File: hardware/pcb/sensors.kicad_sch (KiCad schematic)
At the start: 32 parts, among them J4 4-20mA_1, J5 4-20mA_2, J6 DS18B20, J7 Spare, Q2 BSS123, U9 ADS1115

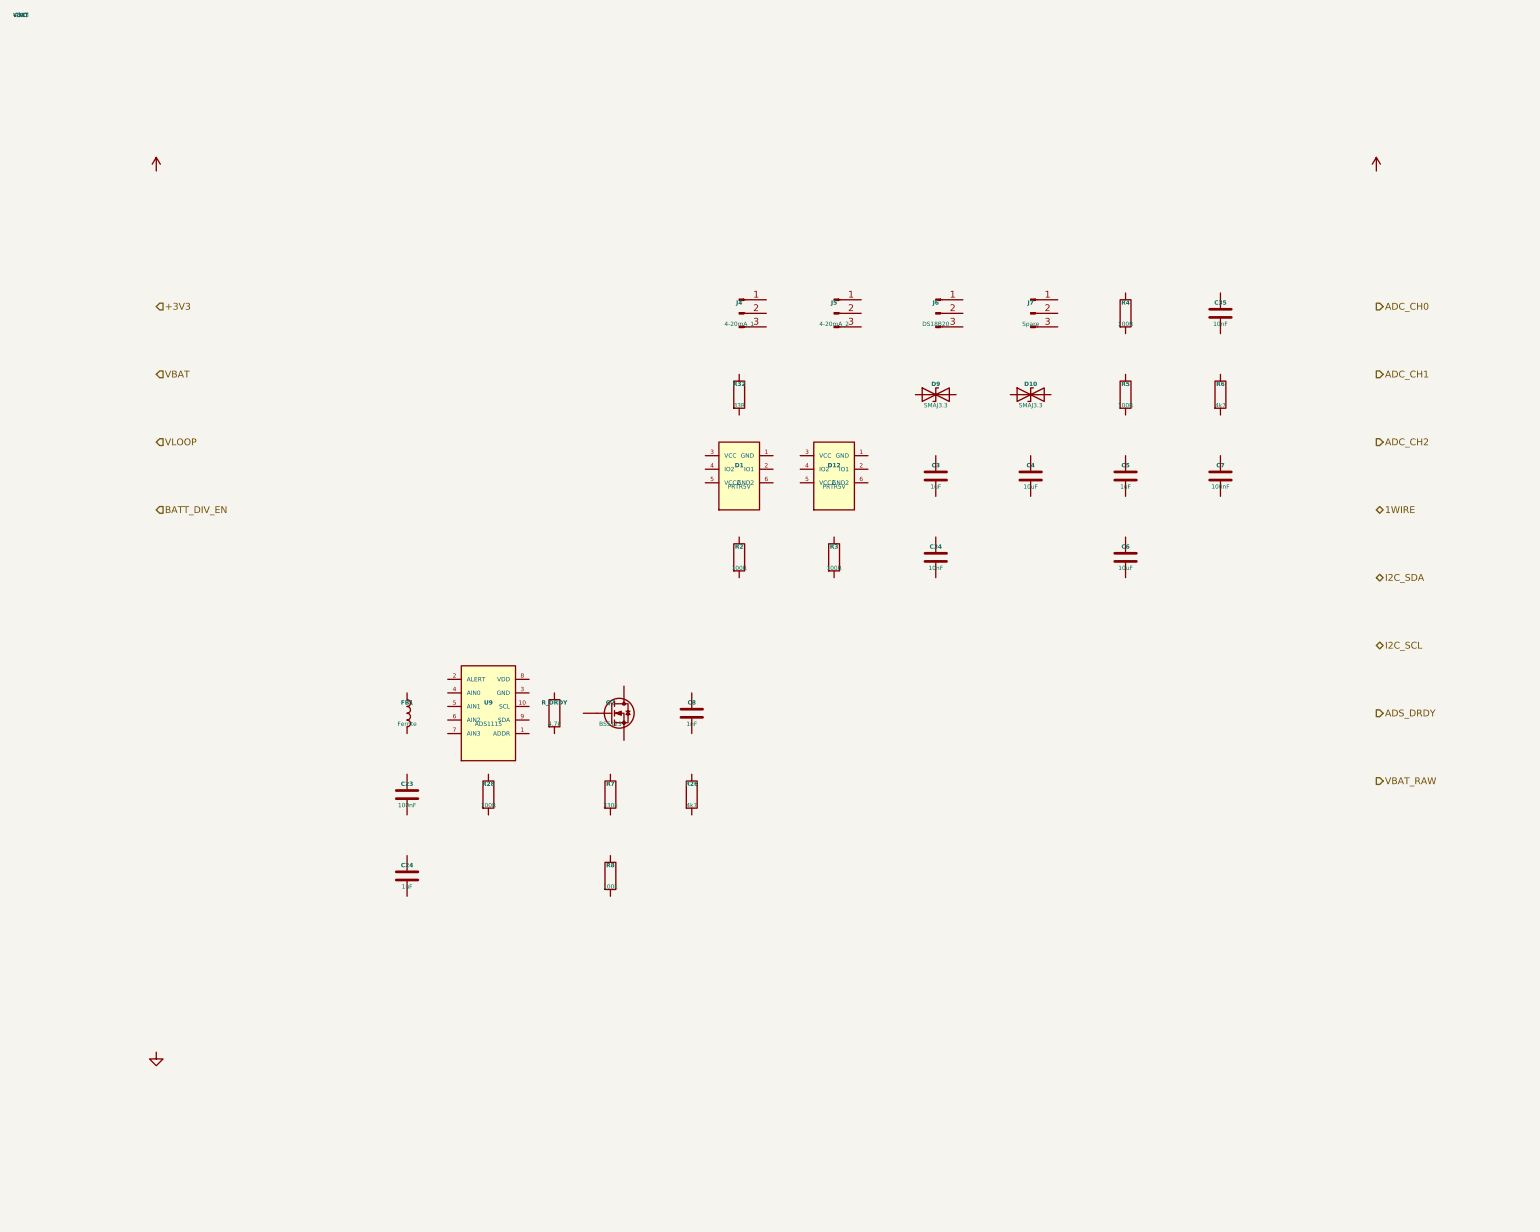
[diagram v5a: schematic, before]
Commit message: hw(pcb): wiring pass — schematic fully wired, netlist machine-verified (0 mismatches)
All four sheets wired with stub+label connectivity (434 wires, 21
explicit no-connects, PWR_FLAGs on undriven rails): power rails on
global labels, cross-sheet signals on hierarchical labels + rebuilt
top-sheet pins (24 hierarchical nets; vestigial ADC_CH* pins deleted,
GPIO14_LED corrected to the mcu-local net it really is), sheet-local
nets on local labels.

Verification (kicad-cli for the KiCad-10 format is not installable
here): hardware/pcb/kicad_wire_script.py generates the connectivity
from an embedded intent table derived from schematic_connections.md;
hardware/pcb/netlist_check.py independently re-extracts pin->net
geometrically (union-find over wires/labels/sheet pins) and diffs —
395 pins, 77 nets, 0 mismatches (output committed). Native KiCad 10
ERC + resave queued for the first interactive open.

Notable resolutions (recorded as design change #17): AP63203 FB tied
to +3V3 with the DNP divider floated at its midpoint; MT3608B pin 6
etype relaxed to passive so C_BST wiring is ERC-legal; IP2326 DM/DP
floated with no-connects (adapter detection is a two-wire future
change); D11 oriented cathode-to-VLOOP; decorative corner power
symbols replaced with real rail connectivity.

placement_constraints.md: Group G rewritten for the IP2326 hot loop,
new Group L for the CN3722 external buck (Kelvin CSP/BAT pair).
Top remaining risk flagged in blockers: AP63203 BST is NC per the
wiring doc but the AP6320x family likely requires a BST-SW cap —
resolve before layout freeze.

Co-Authored-By: Claude Fable 5 <noreply@anthropic.com>
Claude-Session: https://claude.ai/code/session_01VtMFY5Q94iYbsNPpLcPJyK
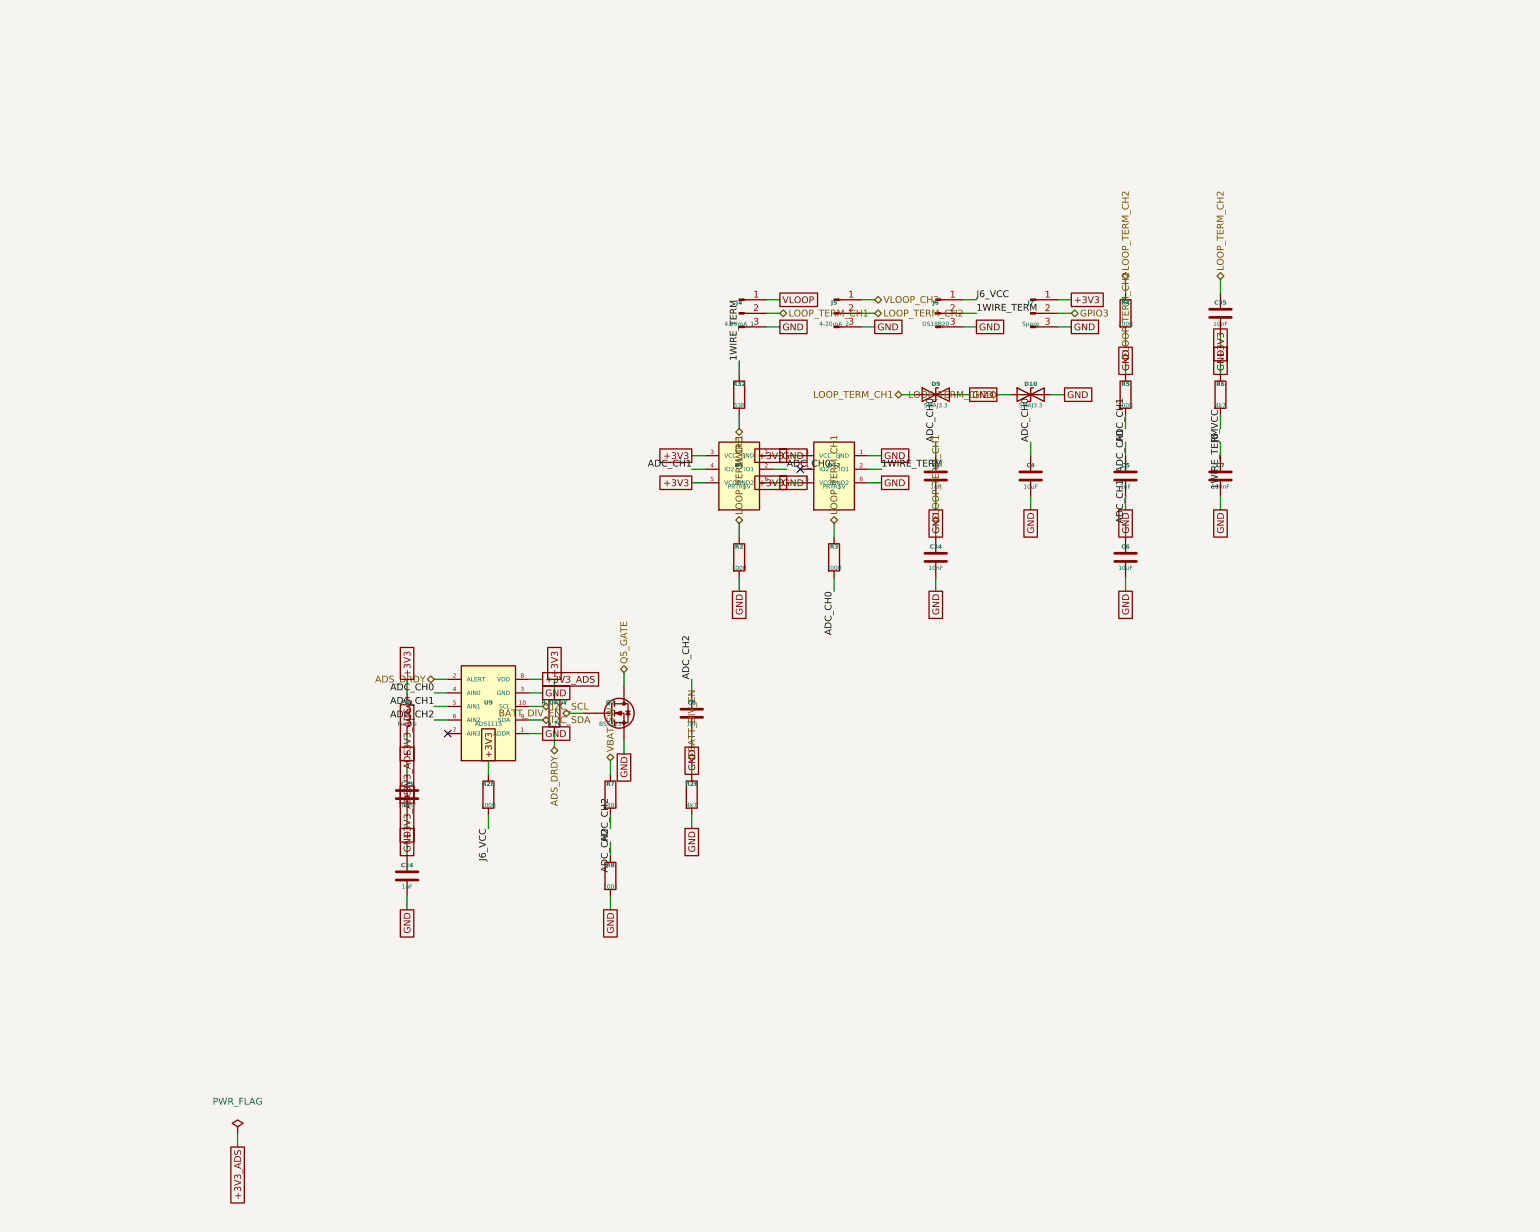
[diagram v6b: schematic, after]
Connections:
- net +3V3: now also D1.3 (VCC), D1.5 (VCC2), D12.3 (VCC), D12.5 (VCC2), FB1.1, J7.1 (Pin_1), R28.1, R6.1, R_DRDY.1
- net 1WIRE: now also R32.2
- net ADC_CH0: now also C3.1, C4.1, D1.2 (IO1), R3.2, U9.4 (AIN0)
- net ADC_CH1: now also C5.1, C6.1, D1.4 (IO2), R5.2, U9.5 (AIN1)
- net ADC_CH2: now also C8.1, R7.2, R8.1, U9.6 (AIN2)
- net ADS_DRDY: now also R_DRDY.2, U9.2 (ALERT)
- net BATT_DIV_EN: now also Q2.G, R26.1
- net GND: now also C23.2, C24.2, C3.2, C34.2, C35.2, C4.2, C5.2, C6.2, C7.2, C8.2, D1.1 (GND), D1.6 (GND2), D10.2 (A2), D12.1 (GND), D12.6 (GND2), D9.2 (A2), J4.3 (Pin_3), J5.3 (Pin_3), J6.3 (Pin_3), J7.3 (Pin_3), Q2.S, R2.2, R26.2, R4.2, R8.2, U9.1 (ADDR), U9.3 (GND)
- net I2C_SCL: now also U9.10 (SCL)
- net I2C_SDA: now also U9.9 (SDA)
- net VLOOP: now also J4.1 (Pin_1)
- net J6_VCC: now reaches C7.1
- net J6_VCC: now also J6.1 (Pin_1), R28.2
- net LOOP_TERM_CH2: now reaches D10.1 (A1)
- net LOOP_TERM_CH2: now also C35.1, J5.2 (Pin_2), R4.1, R5.1
- net LOOP_TERM_CH1: now reaches J4.2 (Pin_2)
- net LOOP_TERM_CH1: now also C34.1, D9.1 (A1), R2.1, R3.1
- net GPIO3: now reaches J7.2 (Pin_2)
- net +3V3_ADS: now reaches U9.8 (VDD)
- net +3V3_ADS: now also C23.1, C24.1, FB1.2
- net VBAT_SW: now reaches R7.1
- net Q5_GATE: now reaches Q2.D
- net 1WIRE_TERM: now reaches R32.1
- net 1WIRE_TERM: now also D12.2 (IO1), J6.2 (Pin_2), R6.2
- net VLOOP_CH2: now reaches J5.1 (Pin_1)
- no-connect marks 0 -> 2

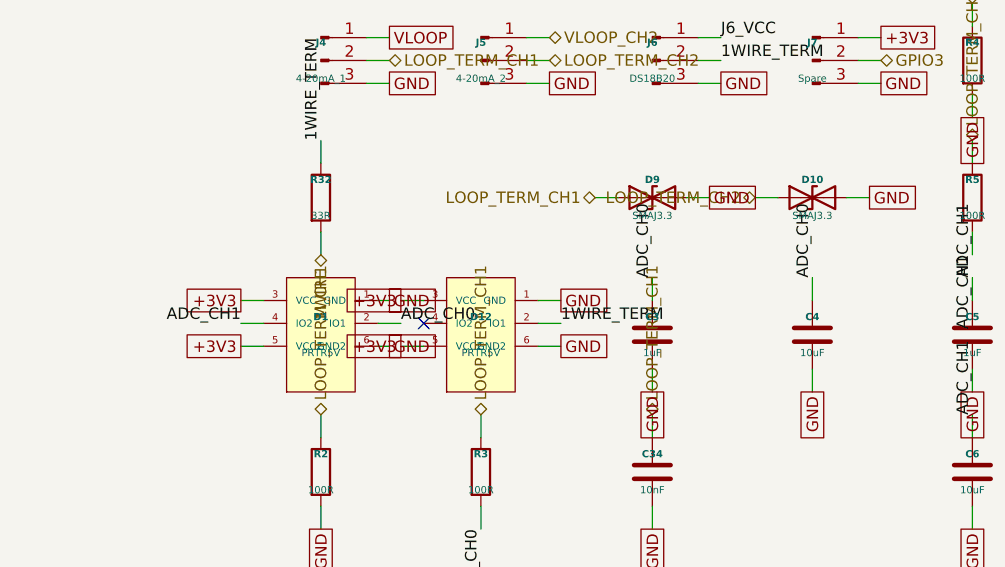
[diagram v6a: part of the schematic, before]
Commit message: hw(pcb): apply blocker #9 — AP63203 renumber + BST cap, ESD symbol fixes, value syncs
All eight required edits from the 2026-07-14 component verification,
applied by pin-name-preserving renumber (positions untouched, so the
stub+label wiring stays electrically identical; only footprint pad
mapping changes):

- U1: lib symbol renamed welld:AP63203WU, pins renumbered to the
  verified Diodes map (FB=1, EN=2, VIN=3, GND=4, SW=5, BST=6),
  footprint TSOT-23-6. NEW C_BST_AP 100 nF placed and wired on new net
  AP_BST (BST <-> SW) — the bootstrap cap without which the 3.3 V rail
  cannot start. BST no_connect removed.
- U11 USBLC6 renumbered to the ST map (I/O1=1, GND=2, I/O2=3, I/O2'=4,
  VBUS=5, I/O1'=6).
- D1/D12 PRTR5V0U2X redrawn as the real 4-pin SOT-143B (GND=1, I/O1=2,
  I/O2=3, VCC=4); phantom VCC2/GND2 pins, their 4 stubs and 4 labels
  removed; instance pin uuids pruned.
- D9/D10 -> SMAJ5.0A; U12 footprint -> QFN-24-1EP_4x4mm_P0.5mm;
  FB1 -> 0603; C28/C29/C_SYS1/C_SYS2 -> 25 V ratings.
- Intent tables in kicad_wire_script.py remapped placeholder-safe;
  netlist_check.py re-run: 393 pins, 78 nets (+AP_BST), 20 no-connects,
  ZERO mismatches. All five sheets pass the balance check.

Co-Authored-By: Claude Fable 5 <noreply@anthropic.com>
Claude-Session: https://claude.ai/code/session_01VtMFY5Q94iYbsNPpLcPJyK
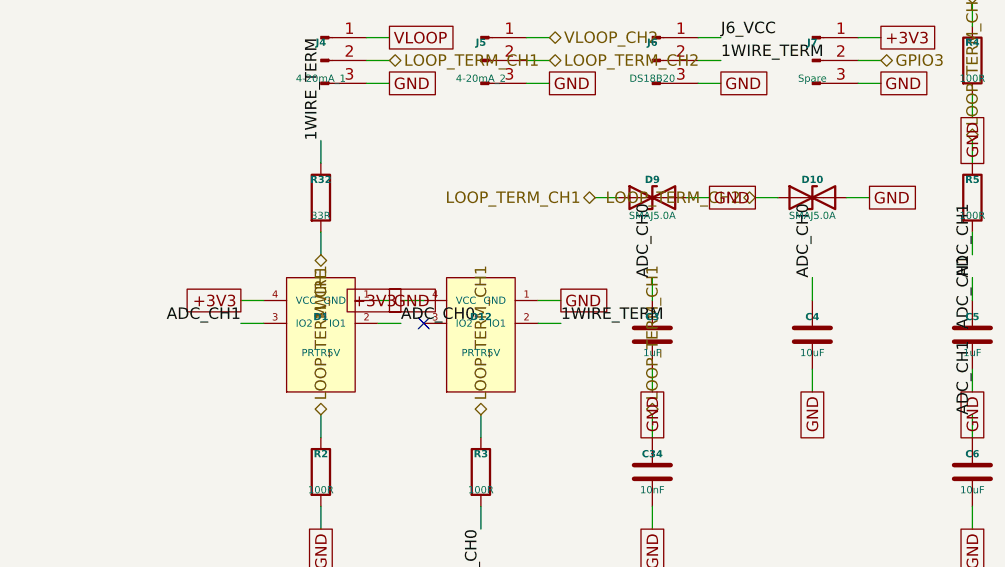
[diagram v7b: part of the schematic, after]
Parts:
- D10, D9: value SMAJ3.3 -> SMAJ5.0A
- FB1: footprint Inductor_SMD:L_0402_1005Metric -> Inductor_SMD:L_0603_1608Metric
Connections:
- net +3V3: now also D1.4 (VCC), D12.4 (VCC); no longer D1.3 (VCC), D1.5 (VCC2), D12.3 (VCC), D12.5 (VCC2)
- net ADC_CH1: now also D1.3 (IO2); no longer D1.4 (IO2)
- net GND: no longer D1.6 (GND2), D12.6 (GND2)
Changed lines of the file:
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@@
 			)
 		)
-		(property "Value" "SMAJ3.3"
+		(property "Value" "SMAJ5.0A"
 			(at 189.23 69.31 0)
 			(show_name no)
@@
 			)
 		)
-		(property "Value" "SMAJ3.3"
+		(property "Value" "SMAJ5.0A"
 			(at 171.45 69.31 0)
 			(show_name no)
@@
 		(pin "4"
 		)
-		(pin "5"
-		)
-		(pin "6"
-		)
 		(instances
 			(project "welld"
@@
 			)
 		)
-		(property "Footprint" "Inductor_SMD:L_0402_1005Metric"
+		(property "Footprint" "Inductor_SMD:L_0603_1608Metric"
 			(at 0 0 0)
 			(hide yes)
@@
 		(pin "4"
 		)
-		(pin "5"
-		)
-		(pin "6"
-		)
 		(instances
 			(project "welld"
@@
 	(wire
 		(pts
-			(xy 128.27 83.82) (xy 125.73 83.82)
-		)
-		(stroke
-			(width 0)
-			(type default)
-		)
-	)
-	(global_label "+3V3"
-		(shape passive)
-		(at 125.73 83.82 180)
-		(fields_autoplaced yes)
-		(effects
-			(font
-				(size 1.27 1.27)
-			)
-			(justify right)
-		)
-		(property "Intersheetrefs" "${INTERSHEET_REFS}"
-			(at 125.73 83.82 0)
-			(hide yes)
-			(show_name no)
-			(do_not_autoplace no)
-			(effects
-				(font
-					(size 1.27 1.27)
-				)
-			)
-		)
-	)
-	(wire
-		(pts
 			(xy 146.05 78.74) (xy 143.51 78.74)
 		)
@@
 	(wire
 		(pts
-			(xy 146.05 83.82) (xy 143.51 83.82)
-		)
-		(stroke
-			(width 0)
-			(type default)
-		)
-	)
-	(global_label "+3V3"
-		(shape passive)
-		(at 143.51 83.82 180)
-		(fields_autoplaced yes)
-		(effects
-			(font
-				(size 1.27 1.27)
-			)
-			(justify right)
-		)
-		(property "Intersheetrefs" "${INTERSHEET_REFS}"
-			(at 143.51 83.82 0)
-			(hide yes)
-			(show_name no)
-			(do_not_autoplace no)
-			(effects
-				(font
-					(size 1.27 1.27)
-				)
-			)
-		)
-	)
-	(wire
-		(pts
 			(xy 194.31 49.53) (xy 196.85 49.53)
 		)
@@
 	(wire
 		(pts
-			(xy 140.97 83.82) (xy 142.24 83.82)
-		)
-		(stroke
-			(width 0)
-			(type default)
-		)
-	)
-	(global_label "GND"
-		(shape passive)
-		(at 142.24 83.82 0)
-		(fields_autoplaced yes)
-		(effects
-			(font
-				(size 1.27 1.27)
-			)
-			(justify left)
-		)
-		(property "Intersheetrefs" "${INTERSHEET_REFS}"
-			(at 142.24 83.82 0)
-			(hide yes)
-			(show_name no)
-			(do_not_autoplace no)
-			(effects
-				(font
-					(size 1.27 1.27)
-				)
-			)
-		)
-	)
-	(wire
-		(pts
 			(xy 158.75 78.74) (xy 161.29 78.74)
 		)
@@
 			(hide yes)
 			(show_name no)
-			(do_not_autoplace no)
-			(effects
-				(font
-					(size 1.27 1.27)
-				)
-			)
-		)
-	)
-	(wire
-		(pts
-			(xy 158.75 83.82) (xy 161.29 83.82)
-		)
-		(stroke
-			(width 0)
-			(type default)
-		)
-	)
-	(global_label "GND"
-		(shape passive)
-		(at 161.29 83.82 0)
-		(fields_autoplaced yes)
-		(effects
-			(font
-				(size 1.27 1.27)
-			)
-			(justify left)
-		)
-		(property "Intersheetrefs" "${INTERSHEET_REFS}"
-			(at 161.29 83.82 0)
-			(hide yes)
-			(show_name no)

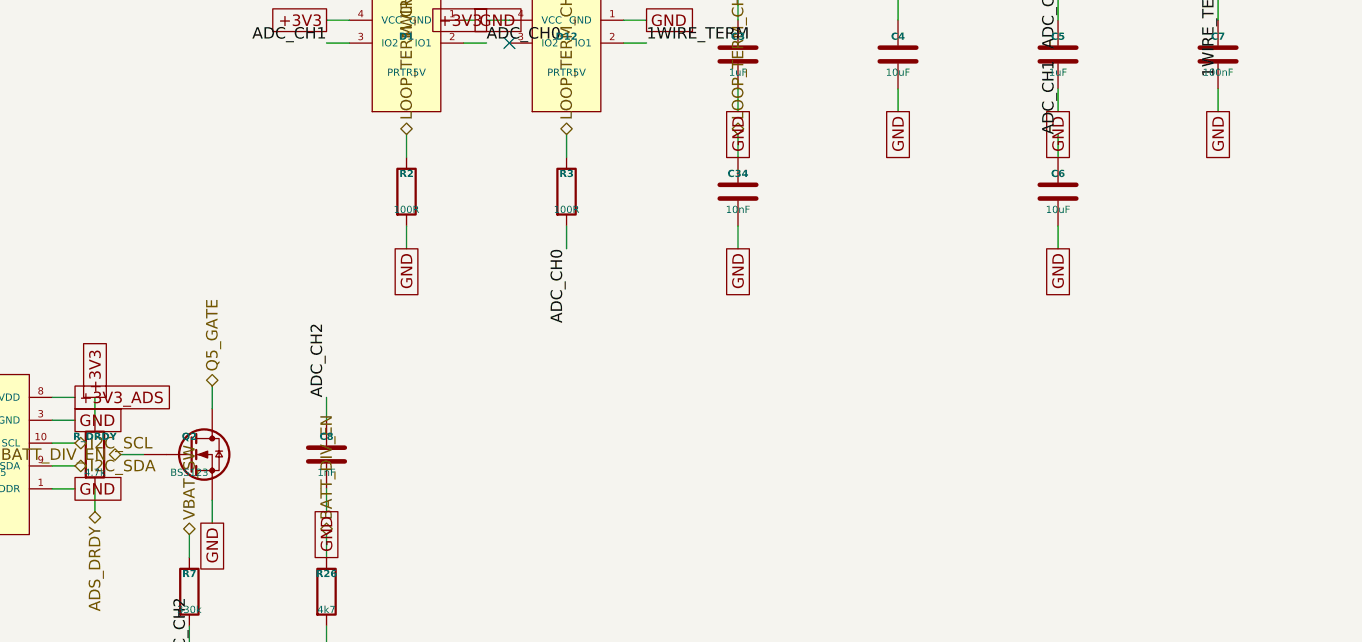
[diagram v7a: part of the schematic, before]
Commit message: hw(pcb): apply approved swaps — AO3400A, SI2319CDS, HRO USB-C, DNF GDT footprints
All four user-approved swaps from the better-options review:
- Q2/Q4 BSS123 -> AO3400A (Vgs(th) max 1.45 V at 3.3 V drive; LCSC
  C20917, 2N7002 second source)
- M_SOLAR AO3407 -> SI2319CDS (-40 V, >60% Vds margin restored; new
  welld:SI2319CDS lib symbol with identical pin geometry; Vishay
  C146287, VBsemi alternate C558254). D5/Q3/Q5 stay AO3407.
- J13 GCT USB4135 -> HRO TYPE-C-31-M-12 (C165948); footprint name
  flagged for verification against the installed KiCad lib; B-side
  mirror-pad net check noted for layout.
- GDT1/GDT2 (DNF, 90 V 2-pole) added on LOOP_TERM_CH1/CH2 to GND —
  completes the industrial GDT->R->TVS surge chain for field wiring;
  populate per site. WellD.pretty land pattern flagged for layout.

netlist_check: 397 pins / 78 nets / 20 NC / zero mismatches; all five
sheets balance. Case note: re-check the USB-C cutout for the HRO shell
once layout places J13. No GPIO or firmware changes.

Co-Authored-By: Claude Fable 5 <noreply@anthropic.com>
Claude-Session: https://claude.ai/code/session_01VtMFY5Q94iYbsNPpLcPJyK
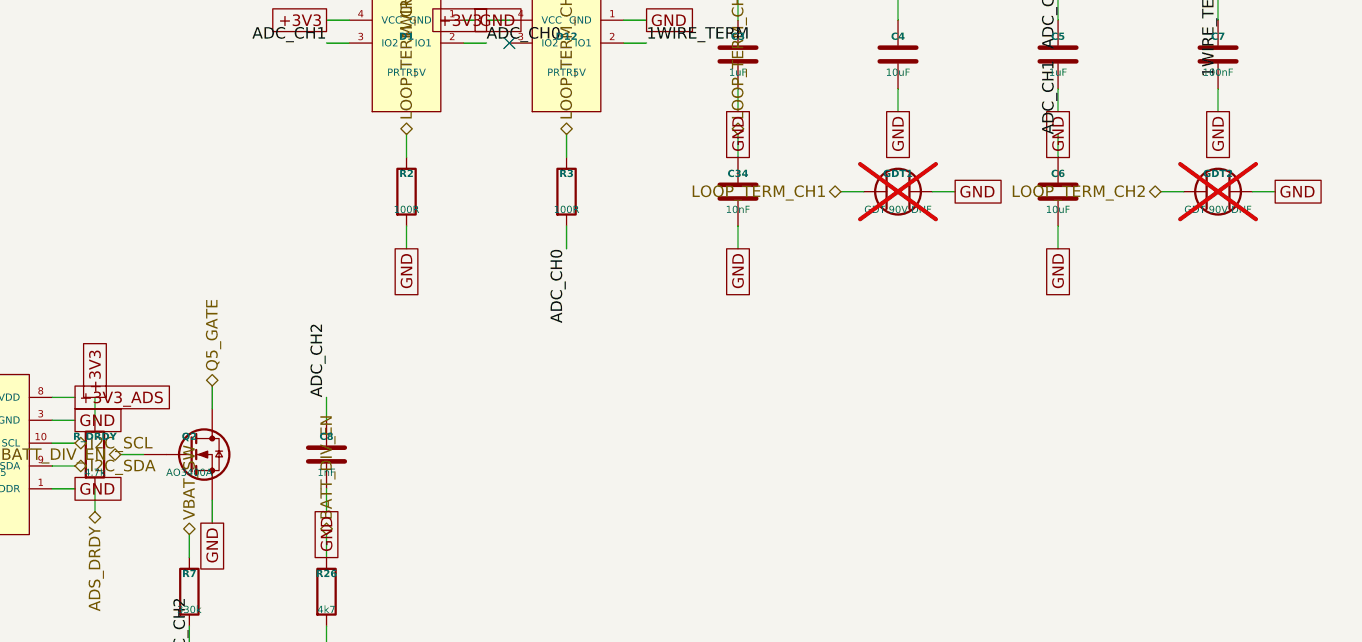
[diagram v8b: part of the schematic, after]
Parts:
- added GDT1, GDT2: GDT 90V DNF, WellD:GDT_BOURNS_2038_SM, symbol welld:GDT
- Q2: value BSS123 -> AO3400A
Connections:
- net GND: now also GDT1.2 (E2), GDT2.2 (E2)
- net LOOP_TERM_CH1: now also GDT1.1 (E1)
- net LOOP_TERM_CH2: now also GDT2.1 (E1)
